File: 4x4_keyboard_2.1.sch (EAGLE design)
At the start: 74 parts, among them U2 AMS1117-5.0

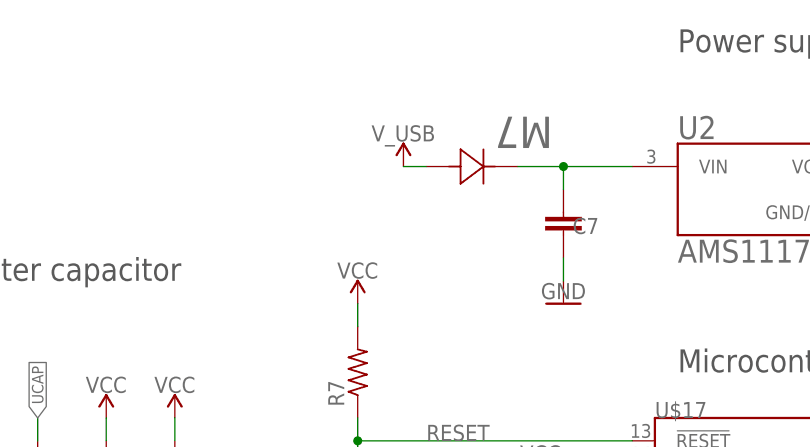
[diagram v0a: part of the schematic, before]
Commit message: Change forward diode package
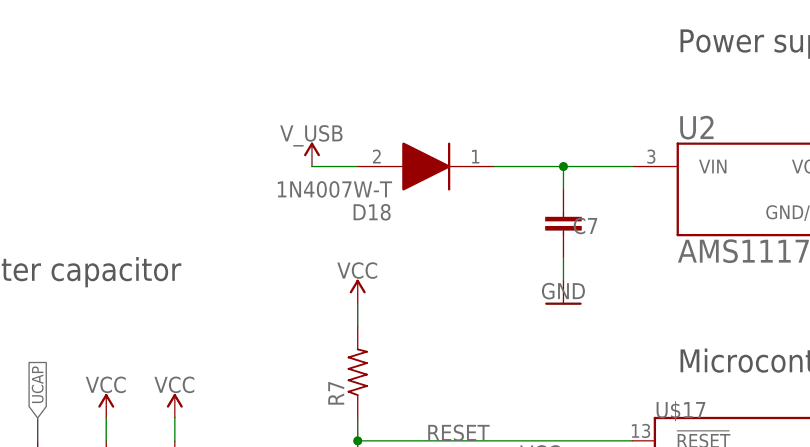
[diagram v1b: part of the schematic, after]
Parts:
- removed CR1: M7, M7 diode:M7
- added D18: 1N4007W-T, 1N4007W-T:1N4007W-T
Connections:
- net N$4: now also D18.K; no longer CR1.2
- net V_USB: now also D18.A; no longer CR1.1
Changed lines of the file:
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@@
 <part name="GND2" library="SparkFun-PowerSymbols" deviceset="GND" device=""/>
 <part name="GND3" library="SparkFun-PowerSymbols" deviceset="GND" device=""/>
-<part name="CR1" library="M7 diode" deviceset="M7" device=""/>
+<part name="D18" library="1N4007W-T" deviceset="1N4007W-T" device=""/>
 </parts>
 <sheets>
@@
 <attribute name="VALUE" x="30.48" y="345.186" size="1.778" layer="96" align="top-center"/>
 </instance>
-<instance part="SUPPLY10" gate="G$1" x="-48.26" y="360.68" smashed="yes">
-<attribute name="VALUE" x="-48.26" y="363.474" size="1.778" layer="96" align="bottom-center"/>
+<instance part="SUPPLY10" gate="G$1" x="-58.42" y="360.68" smashed="yes">
+<attribute name="VALUE" x="-58.42" y="363.474" size="1.778" layer="96" align="bottom-center"/>
 </instance>
 <instance part="U$1" gate="G$1" x="66.04" y="330.2" smashed="yes" rot="R180">
@@
 <attribute name="VALUE" x="17.78" y="347.726" size="1.778" layer="96" align="top-center"/>
 </instance>
-<instance part="CR1" gate="A" x="-35.56" y="360.68" smashed="yes" rot="R180">
-<attribute name="VALUE" x="-31.6738" y="366.2172" size="3.4798" layer="96" ratio="10" rot="SR180"/>
+<instance part="D18" gate="G$1" x="-38.1" y="360.68" smashed="yes" rot="R180">
+<attribute name="NAME" x="-49.53" y="355.6" size="1.778" layer="95" rot="R180" align="center-left"/>
+<attribute name="VALUE" x="-49.53" y="358.14" size="1.778" layer="96" rot="R180" align="center-left"/>
 </instance>
 </instances>
@@
 <segment>
 <pinref part="SUPPLY10" gate="G$1" pin="V_USB"/>
-<wire x1="-48.26" y1="360.68" x2="-45.72" y2="360.68" width="0.1524" layer="91"/>
-<pinref part="CR1" gate="A" pin="1"/>
+<wire x1="-53.34" y1="360.68" x2="-58.42" y2="360.68" width="0.1524" layer="91"/>
+<pinref part="D18" gate="G$1" pin="A"/>
 </segment>
 <segment>
@@
 <segment>
 <pinref part="U2" gate="G$1" pin="VIN"/>
-<pinref part="CR1" gate="A" pin="2"/>
 <wire x1="-22.86" y1="360.68" x2="-30.48" y2="360.68" width="0.1524" layer="91"/>
 <pinref part="C7" gate="G$1" pin="2"/>
-<wire x1="-30.48" y1="360.68" x2="-35.56" y2="360.68" width="0.1524" layer="91"/>
+<wire x1="-30.48" y1="360.68" x2="-38.1" y2="360.68" width="0.1524" layer="91"/>
 <wire x1="-30.48" y1="358.14" x2="-30.48" y2="360.68" width="0.1524" layer="91"/>
 <junction x="-30.48" y="360.68"/>
-</segment>
-</net>
+<pinref part="D18" gate="G$1" pin="K"/>
+</segment>
+</net>

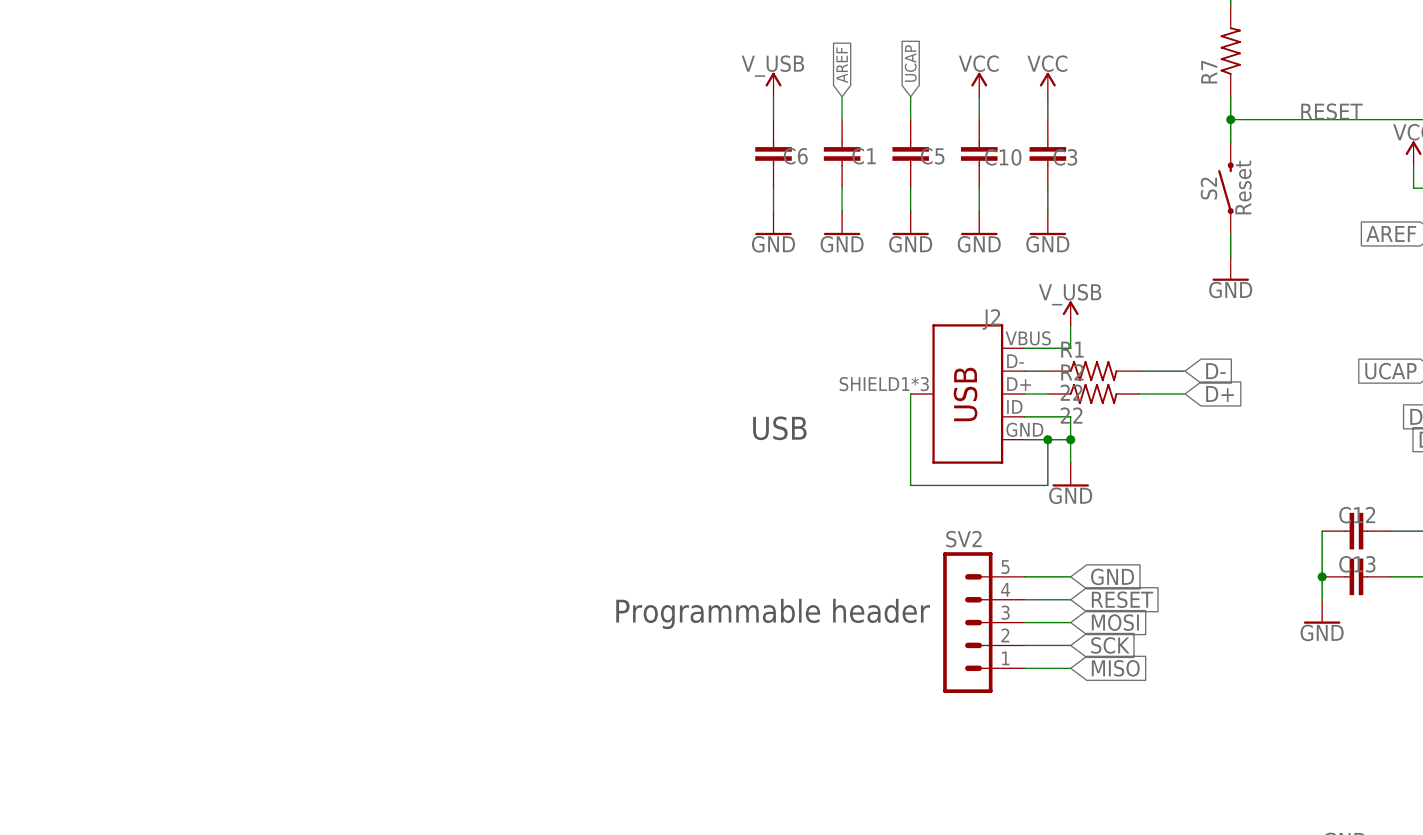
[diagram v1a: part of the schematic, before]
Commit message: Added the usb c and usb A package
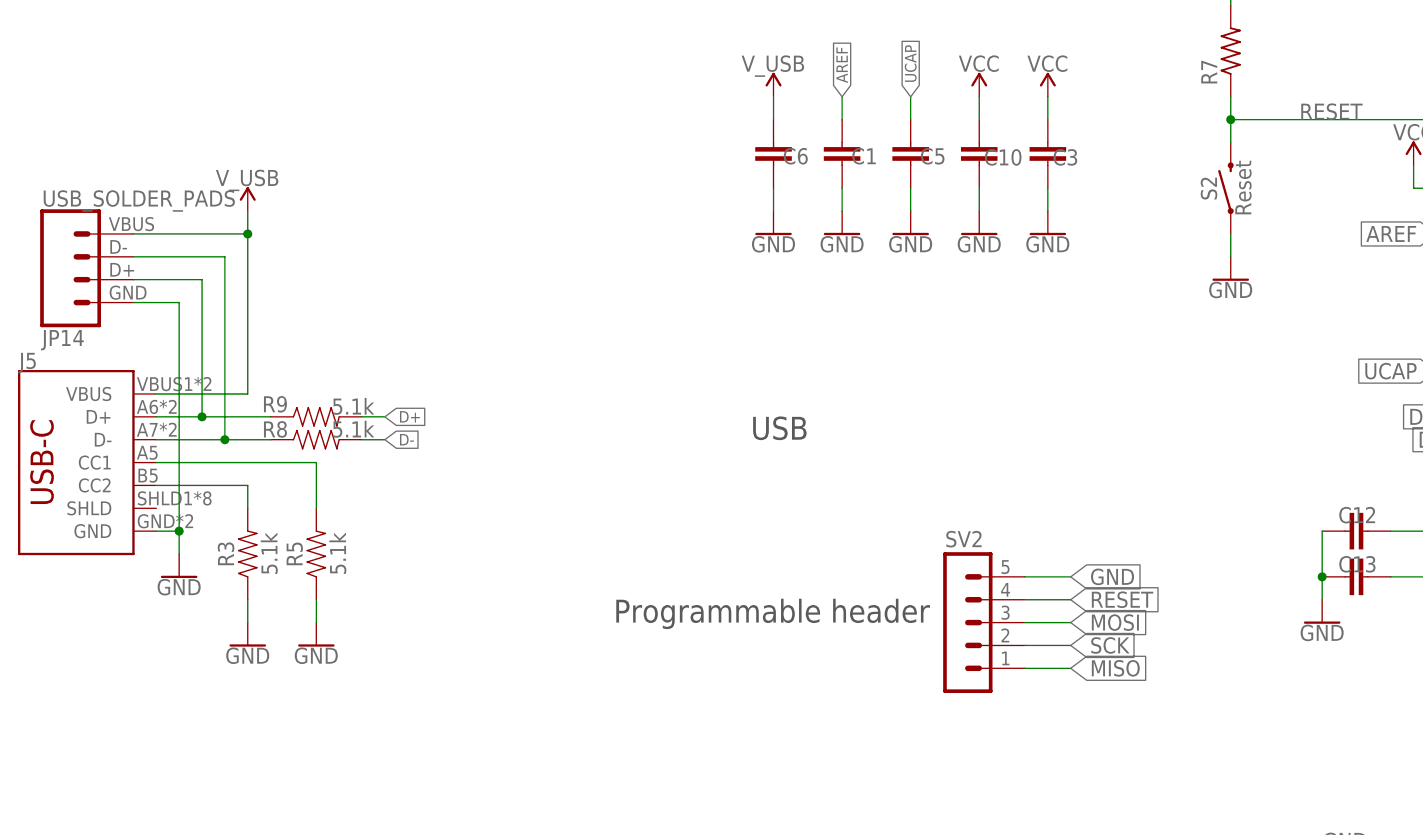
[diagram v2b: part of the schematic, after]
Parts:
- removed J2: (no value), SparkFun-Connectors:USB_MICRO-B_FEMALE-SMT
- removed R1, R2: 22, audio amplifier example:R-US_R0603
- added J5: (no value), USBC:USB_C5
- added JP14: USB_SOLDER_PADS, SparkFun-Connectors:USB_SOLDER_PADS
- added R3, R5, R8, R9: 5.1k, SparkFun-Resistors:5.1KOHM-0402T-1/16W-1%
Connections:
- removed net N$1: J2.D-, R1.1
- removed net N$3: J2.D+, R2.1
- new net D-_HV: J5.D-, JP14.2, R8.1
- new net DP_HV: J5.D+, JP14.3, R9.1
- new net N$13: J5.CC2, R3.2
- new net N$7: J5.CC1, R5.2
- net D+: now also R9.2; no longer R2.2
- net D-: now also R8.2; no longer R1.2
- net GND: now also J5.GND, JP14.4, R3.1, R5.1; no longer J2.GND, J2.ID, J2.SHIELD
- net V_USB: now also J5.VBUS, JP14.1; no longer J2.VBUS

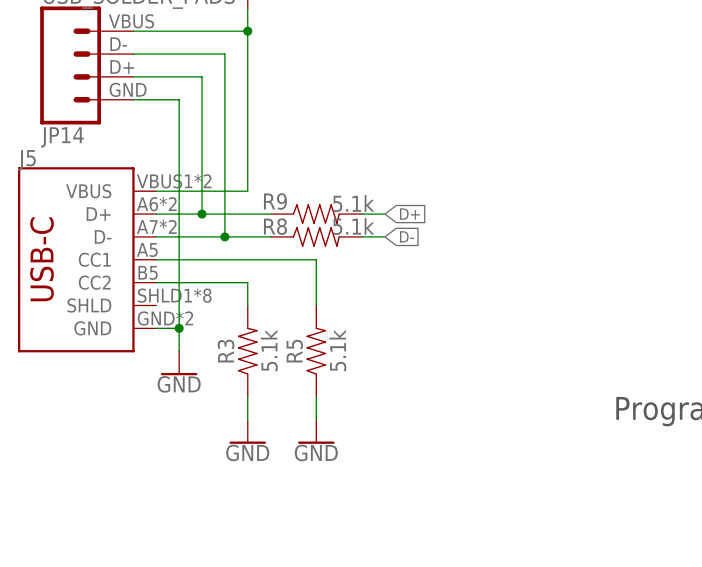
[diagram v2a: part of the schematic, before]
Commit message: USB C is connect and final output without error
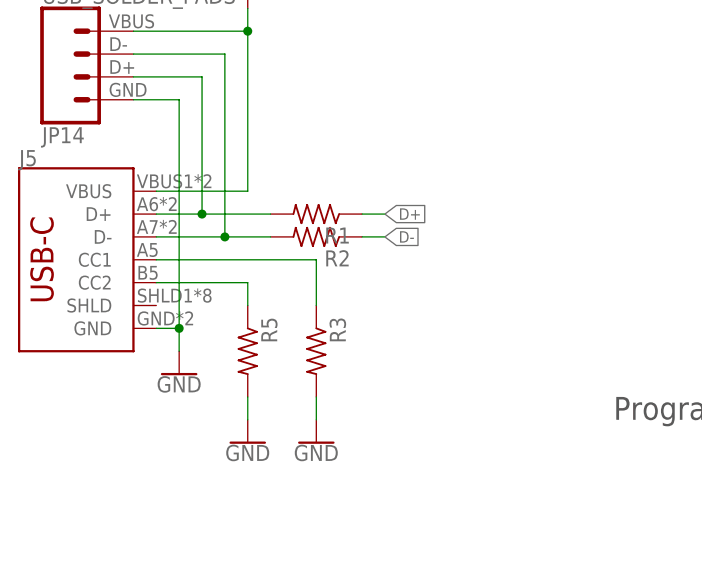
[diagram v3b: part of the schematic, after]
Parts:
- removed R8, R9: 5.1k, SparkFun-Resistors:5.1KOHM-0402T-1/16W-1%
- added R1, R2: 5.1k, audio amplifier example:R-US_R0603
- R3, R5: device SparkFun-Resistors:5.1KOHM-0402T-1/16W-1% -> audio amplifier example:R-US_R0603
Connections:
- net D+: now also R1.1; no longer R9.2
- net D-: now also R2.1; no longer R8.2
- net D-_HV: now also R2.2; no longer R8.1
- net DP_HV: now also R1.2; no longer R9.1
- net GND: now also R3.2, R5.2; no longer R3.1, R5.1
- net N$13: now also R5.1; no longer R3.2
- net N$7: now also R3.1; no longer R5.2
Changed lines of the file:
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@@
 <part name="D18" library="1N4007W-T" deviceset="1N4007W-T" device=""/>
 <part name="GND14" library="SparkFun-PowerSymbols" deviceset="GND" device=""/>
-<part name="R3" library="SparkFun-Resistors" deviceset="5.1KOHM" device="-0402T-1/16W-1%" value="5.1k"/>
-<part name="R5" library="SparkFun-Resistors" deviceset="5.1KOHM" device="-0402T-1/16W-1%" value="5.1k"/>
 <part name="GND15" library="SparkFun-PowerSymbols" deviceset="GND" device=""/>
 <part name="GND19" library="SparkFun-PowerSymbols" deviceset="GND" device=""/>
 <part name="SUPPLY2" library="SparkFun-PowerSymbols" deviceset="V_USB" device=""/>
-<part name="R8" library="SparkFun-Resistors" deviceset="5.1KOHM" device="-0402T-1/16W-1%" value="5.1k"/>
-<part name="R9" library="SparkFun-Resistors" deviceset="5.1KOHM" device="-0402T-1/16W-1%" value="5.1k"/>
 <part name="JP14" library="SparkFun-Connectors" deviceset="USB_SOLDER_PADS" device=""/>
 <part name="J5" library="USBC" deviceset="USB_C" device="5"/>
+<part name="R1" library="audio amplifier example" deviceset="R-US_" device="R0603" value="5.1k"/>
+<part name="R2" library="audio amplifier example" deviceset="R-US_" device="R0603" value="5.1k"/>
+<part name="R3" library="audio amplifier example" deviceset="R-US_" device="R0603" value="5.1k"/>
+<part name="R5" library="audio amplifier example" deviceset="R-US_" device="R0603" value="5.1k"/>
 </parts>
 <sheets>
@@
 <attribute name="VALUE" x="-170.18" y="279.146" size="1.778" layer="96" align="top-center"/>
 </instance>
-<instance part="R3" gate="R1" x="-162.56" y="281.94" smashed="yes" rot="R90">
-<attribute name="NAME" x="-164.084" y="281.94" size="1.778" layer="95" font="vector" rot="R90" align="bottom-center"/>
-<attribute name="VALUE" x="-161.036" y="281.94" size="1.778" layer="96" font="vector" rot="R90" align="top-center"/>
-</instance>
-<instance part="R5" gate="R1" x="-154.94" y="281.94" smashed="yes" rot="R90">
-<attribute name="NAME" x="-156.464" y="281.94" size="1.778" layer="95" font="vector" rot="R90" align="bottom-center"/>
-<attribute name="VALUE" x="-153.416" y="281.94" size="1.778" layer="96" font="vector" rot="R90" align="top-center"/>
-</instance>
 <instance part="GND15" gate="1" x="-162.56" y="271.78" smashed="yes">
 <attribute name="VALUE" x="-162.56" y="271.526" size="1.778" layer="96" align="top-center"/>
@@
 <instance part="SUPPLY2" gate="G$1" x="-162.56" y="320.04" smashed="yes">
 <attribute name="VALUE" x="-162.56" y="322.834" size="1.778" layer="96" align="bottom-center"/>
-</instance>
-<instance part="R8" gate="R1" x="-154.94" y="294.64" smashed="yes">
-<attribute name="NAME" x="-159.512" y="294.894" size="1.778" layer="95" font="vector" align="bottom-center"/>
-<attribute name="VALUE" x="-150.876" y="294.894" size="1.778" layer="96" font="vector" rot="R180" align="top-center"/>
-</instance>
-<instance part="R9" gate="R1" x="-154.94" y="297.18" smashed="yes">
-<attribute name="NAME" x="-159.512" y="297.688" size="1.778" layer="95" font="vector" align="bottom-center"/>
-<attribute name="VALUE" x="-150.876" y="297.434" size="1.778" layer="96" font="vector" rot="R180" align="top-center"/>
 </instance>
 <instance part="JP14" gate="JP1" x="-180.34" y="314.96" smashed="yes" rot="MR180">
@@
 <attribute name="VALUE" x="-187.96" y="279.654" size="1.778" layer="96" font="vector" rot="MR180" align="top-left"/>
 <attribute name="NAME" x="-187.96" y="302.514" size="1.778" layer="95" font="vector"/>
+</instance>
+<instance part="R1" gate="G$1" x="-154.94" y="297.18" smashed="yes" rot="R180">
+<attribute name="NAME" x="-151.13" y="295.6814" size="1.778" layer="95" rot="R180"/>
+</instance>
+<instance part="R2" gate="G$1" x="-154.94" y="294.64" smashed="yes" rot="R180">
+<attribute name="NAME" x="-151.13" y="293.1414" size="1.778" layer="95" rot="R180"/>
+</instance>
+<instance part="R3" gate="G$1" x="-154.94" y="281.94" smashed="yes" rot="R270">
+<attribute name="NAME" x="-153.4414" y="285.75" size="1.778" layer="95" rot="R270"/>
+</instance>
+<instance part="R5" gate="G$1" x="-162.56" y="281.94" smashed="yes" rot="R270">
+<attribute name="NAME" x="-161.0614" y="285.75" size="1.778" layer="95" rot="R270"/>
 </instance>
 </instances>
@@
 </segment>
 <segment>
-<pinref part="R3" gate="R1" pin="1"/>
 <pinref part="GND15" gate="1" pin="GND"/>
 <wire x1="-162.56" y1="274.32" x2="-162.56" y2="276.86" width="0.1524" layer="91"/>
-</segment>
-<segment>
-<pinref part="R5" gate="R1" pin="1"/>
+<pinref part="R5" gate="G$1" pin="2"/>
+</segment>
+<segment>
 <pinref part="GND19" gate="1" pin="GND"/>
 <wire x1="-154.94" y1="274.32" x2="-154.94" y2="276.86" width="0.1524" layer="91"/>
+<pinref part="R3" gate="G$1" pin="2"/>
 </segment>
 </net>
@@
 <wire x1="-149.86" y1="294.64" x2="-147.32" y2="294.64" width="0.1524" layer="91"/>
 <label x="-147.32" y="294.64" size="1.27" layer="95" xref="yes"/>
-<pinref part="R8" gate="R1" pin="2"/>
+<pinref part="R2" gate="G$1" pin="1"/>
 </segment>
 </net>
@@
 <wire x1="-149.86" y1="297.18" x2="-147.32" y2="297.18" width="0.1524" layer="91"/>
 <label x="-147.32" y="297.18" size="1.27" layer="95" xref="yes"/>
-<pinref part="R9" gate="R1" pin="2"/>
+<pinref part="R1" gate="G$1" pin="1"/>
 </segment>
 </net>
@@
 <segment>
 <wire x1="-172.72" y1="294.64" x2="-165.1" y2="294.64" width="0.1524" layer="91"/>
-<pinref part="R8" gate="R1" pin="1"/>
 <pinref part="JP14" gate="JP1" pin="2"/>
 <wire x1="-165.1" y1="294.64" x2="-160.02" y2="294.64" width="0.1524" layer="91"/>
@@
 <junction x="-165.1" y="294.64"/>
 <pinref part="J5" gate="J1" pin="D-"/>
+<pinref part="R2" gate="G$1" pin="2"/>
 </segment>
 </net>
@@
 <segment>
 <wire x1="-172.72" y1="297.18" x2="-167.64" y2="297.18" width="0.1524" layer="91"/>
-<pinref part="R9" gate="R1" pin="1"/>
 <pinref part="JP14" gate="JP1" pin="3"/>
 <wire x1="-167.64" y1="297.18" x2="-160.02" y2="297.18" width="0.1524" layer="91"/>
@@
 <junction x="-167.64" y="297.18"/>
 <pinref part="J5" gate="J1" pin="D+"/>
+<pinref part="R1" gate="G$1" pin="2"/>
 </segment>
 </net>
 <net name="N$7" class="0">
 <segment>
-<pinref part="R5" gate="R1" pin="2"/>
 <wire x1="-172.72" y1="292.1" x2="-154.94" y2="292.1" width="0.1524" layer="91"/>
 <wire x1="-154.94" y1="292.1" x2="-154.94" y2="287.02" width="0.1524" layer="91"/>
 <pinref part="J5" gate="J1" pin="CC1"/>
+<pinref part="R3" gate="G$1" pin="1"/>
 </segment>
 </net>
 <net name="N$13" class="0">
 <segment>
-<pinref part="R3" gate="R1" pin="2"/>
 <wire x1="-172.72" y1="289.56" x2="-162.56" y2="289.56" width="0.1524" layer="91"/>
 <wire x1="-162.56" y1="289.56" x2="-162.56" y2="287.02" width="0.1524" layer="91"/>
 <pinref part="J5" gate="J1" pin="CC2"/>
-</segment>
-</net>
+<pinref part="R5" gate="G$1" pin="1"/>
+</segment>
+</net>
